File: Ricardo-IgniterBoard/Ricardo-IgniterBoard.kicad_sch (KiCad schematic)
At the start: 39 parts, among them J1 RBUS, U1 ESP32-S3, Y1 R940000171

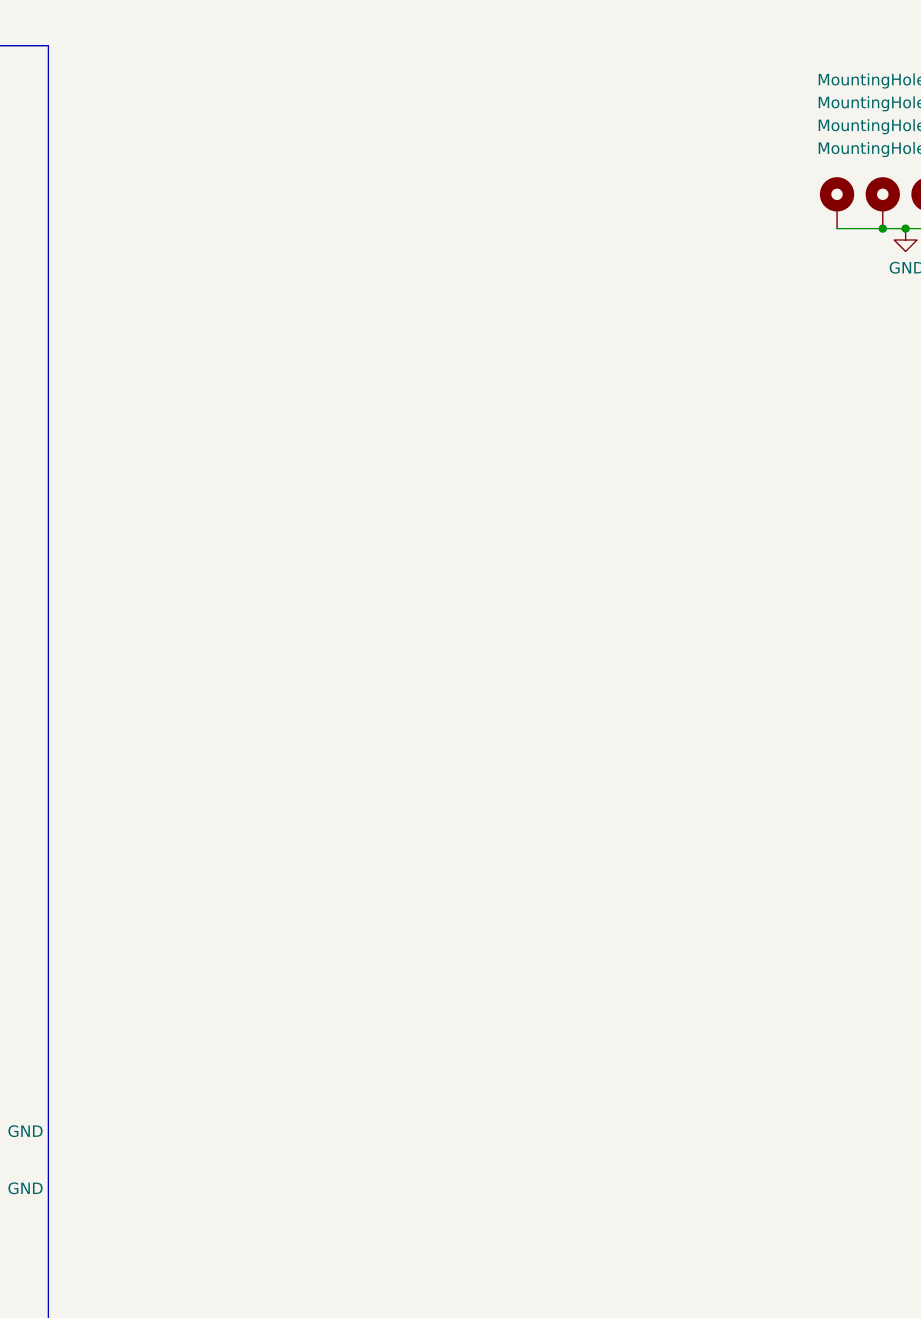
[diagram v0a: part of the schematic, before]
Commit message: Adding pre-existing sheets
Added pyro, high-side master switch and pt sensor
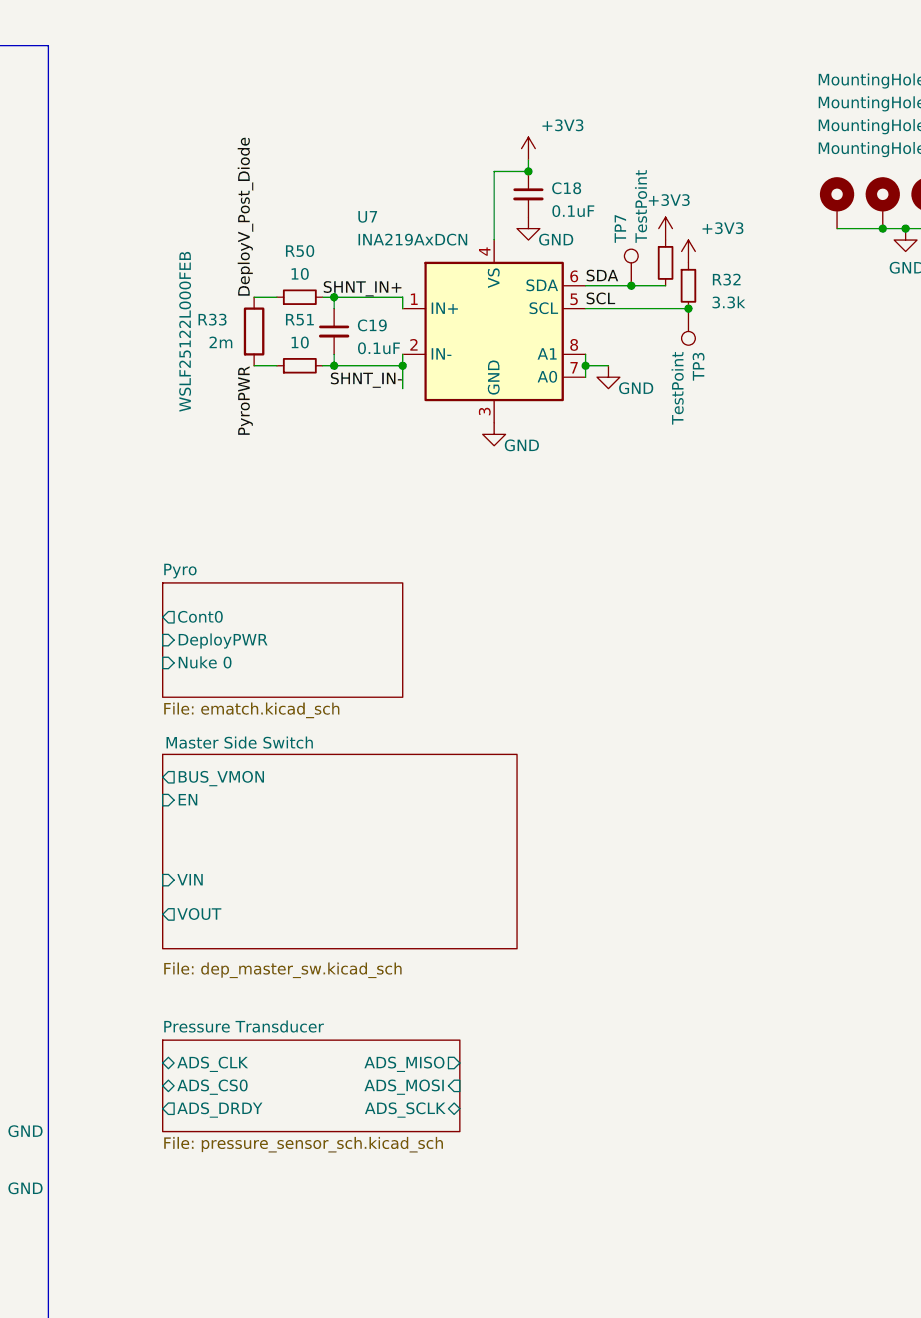
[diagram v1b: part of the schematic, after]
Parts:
- added C18, C19: 0.1uF, Capacitor_SMD:C_0402_1005Metric, symbol Device:C_Small
- added R31, R32: 3.3k, Resistor_SMD:R_0402_1005Metric, symbol Device:R_Small
- added R33: 2m, Resistor_SMD:R_2512_6332Metric_Pad1.40x3.35mm_HandSolder, symbol Device:R
- added R50, R51: 10, Resistor_SMD:R_0402_1005Metric, symbol Device:R_Small
- added TP3, TP7: TestPoint, TestPoint:TestPoint_Pad_D1.0mm, symbol Connector:TestPoint
- added U7: INA219AxDCN, Package_TO_SOT_SMD:SOT-23-8, symbol Sensor_Energy:INA219AxDCN
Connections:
- net +3V3: now also C18.1, R31.1, R32.1, U7.4 (VS)
- net GND: now also C18.2, U7.3 (GND), U7.7 (A0), U7.8 (A1)
- new net DeployV_Post_Diode: R33.1, R50.1
- new net PyroPWR: R33.2, R51.1
- new net SCL: R32.2, TP3.1, U7.5 (SCL)
- new net SDA: R31.2, TP7.1, U7.6 (SDA)
- new net SHNT_IN+: C19.1, R50.2, U7.1 (IN+)
- new net SHNT_IN-: C19.2, R51.2, U7.2 (IN-)
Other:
- added sheet Master Side Switch (dep_master_sw.kicad_sch)
- added sheet Pressure Transducer (pressure_sensor_sch.kicad_sch)
- added sheet Pyro (ematch.kicad_sch)

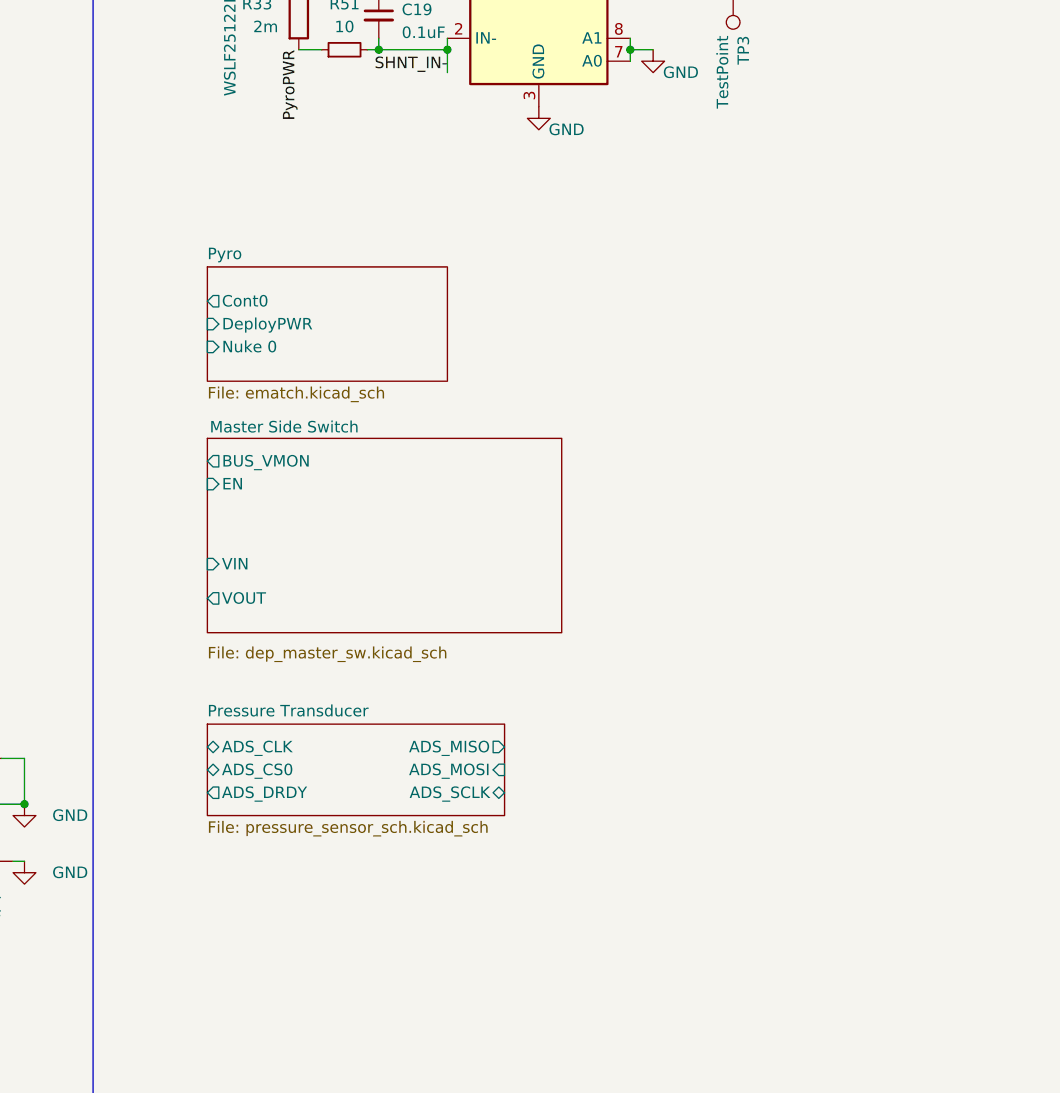
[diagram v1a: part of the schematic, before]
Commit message: Adjusting numbers and adding hieratical pins
Adjusted number of pyro and PT modules and connected everything to the root
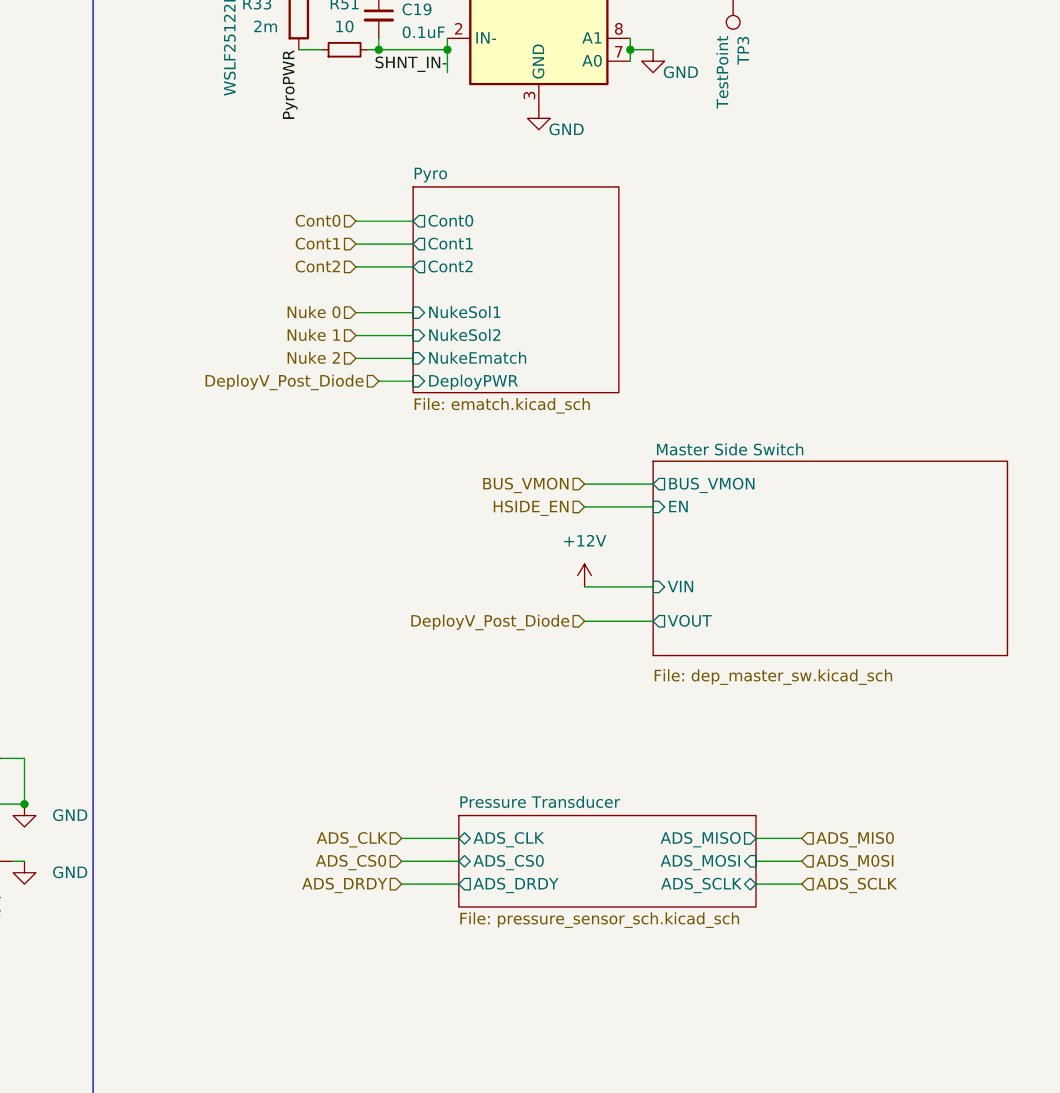
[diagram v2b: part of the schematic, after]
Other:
- sheet Pyro ports: added Cont1, Cont2, NukeEmatch, NukeSol1, NukeSol2; removed Nuke 0

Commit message: Added Voltage Regulator
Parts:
- added R52: 10k, Resistor_SMD:R_0402_1005Metric, symbol Device:R_Small
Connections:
- net BUS_VMON: now also U1.13 (GPIO8/ADC1_CH7)
- net CAN_RX: now also U1.23 (GPIO17/ADC2_CH6/DAC_2)
- net CAN_TX: now also U1.24 (GPIO18/ADC2_CH7/DAC_1)
- net Cont0: now also U1.42 (GPIO37)
- net Cont1: now also U1.43 (GPIO38)
- net Cont2: now also U1.37 (SPICLK_P/GPIO47)
- net GND: now also R52.1
- net HSIDE_EN: now also U1.14 (GPIO9/ADC1_CH8)
- net PyroPWR: now also R52.2
- net SCL: now also U1.16 (GPIO11/ADC2_CH0)
- net SDA: now also U1.15 (GPIO10/ADC1_CH9)
- net CurrentSense: now reaches U1.17 (GPIO12/ADC2_CH1)
- net BuckBoostProt: now reaches U1.18 (GPIO13/ADC2_CH2)
- net Nuke2: now reaches U1.38 (GPIO33)
- net Nuke1: now reaches U1.39 (GPIO34)
- net Nuke0: now reaches U1.40 (GPIO35)
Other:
- added sheet Voltage Regulator (BuckBoost.kicad_sch)

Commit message: Little touches
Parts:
- removed C18, C19: 0.1uF, Capacitor_SMD:C_0402_1005Metric, symbol Device:C_Small
- removed R31, R32: 3.3k, Resistor_SMD:R_0402_1005Metric, symbol Device:R_Small
- removed R33: 2m, Resistor_SMD:R_2512_6332Metric_Pad1.40x3.35mm_HandSolder, symbol Device:R
- removed R50, R51: 10, Resistor_SMD:R_0402_1005Metric, symbol Device:R_Small
- removed R52: 10k, Resistor_SMD:R_0402_1005Metric, symbol Device:R_Small
- removed TP3, TP7: TestPoint, TestPoint:TestPoint_Pad_D1.0mm, symbol Connector:TestPoint
- removed U7: INA219AxDCN, Package_TO_SOT_SMD:SOT-23-8, symbol Sensor_Energy:INA219AxDCN
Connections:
- net ADS_CLK: now also U1.7 (GPIO2/ADC1_CH1)
- net ADS_CS0: now also U1.10 (GPIO5/ADC1_CH4)
- net ADS_DRDY: now also U1.11 (GPIO6/ADC1_CH5)
- net ADS_MISO: now also U1.12 (GPIO7/ADC1_CH6)
- net ADS_MOSI: now also U1.13 (GPIO8/ADC1_CH7)
- net ADS_SCLK: now also U1.9 (GPIO4/ADC1_CH3)
- net BUS_VMON: now also U1.14 (GPIO9/ADC1_CH8); no longer U1.13 (GPIO8/ADC1_CH7)
- net BuckBoostProt: now also U1.19 (GPIO14/ADC2_CH3); no longer U1.18 (GPIO13/ADC2_CH2)
- net Cont2: now also U1.51 (GPIO45); no longer U1.37 (SPICLK_P/GPIO47)
- net CurrentSense: now also U1.18 (GPIO13/ADC2_CH2); no longer U1.17 (GPIO12/ADC2_CH1)
- net HSIDE_EN: now also U1.15 (GPIO10/ADC1_CH9); no longer U1.14 (GPIO9/ADC1_CH8)
- net SCL: now also U1.17 (GPIO12/ADC2_CH1); no longer U1.16 (GPIO11/ADC2_CH0)
- net SDA: now also U1.16 (GPIO11/ADC2_CH0); no longer U1.15 (GPIO10/ADC1_CH9)
- no-connect marks 11 -> 22
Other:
- note added: "Possibly need a series termination resistor on ADS_CLK"
